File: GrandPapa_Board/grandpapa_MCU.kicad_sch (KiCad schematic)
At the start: 19 parts, among them J6 Conn_02x06, U10 MCP2515, U8 PIC18F26K83, Y1 12MHz

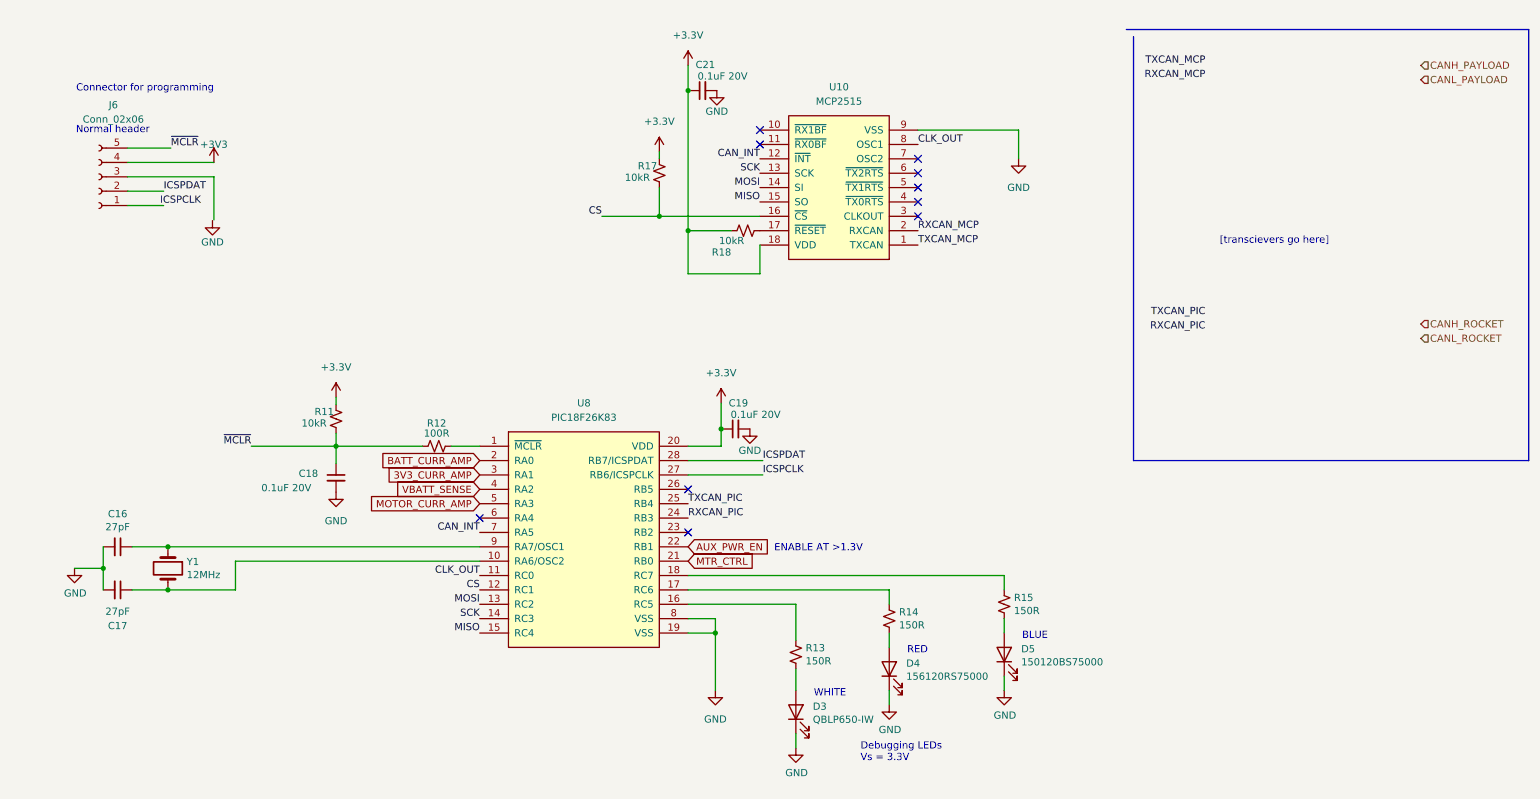
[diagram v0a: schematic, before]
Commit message: Remove 3.3V, placeholders for battery charge IC and 5V boost converter
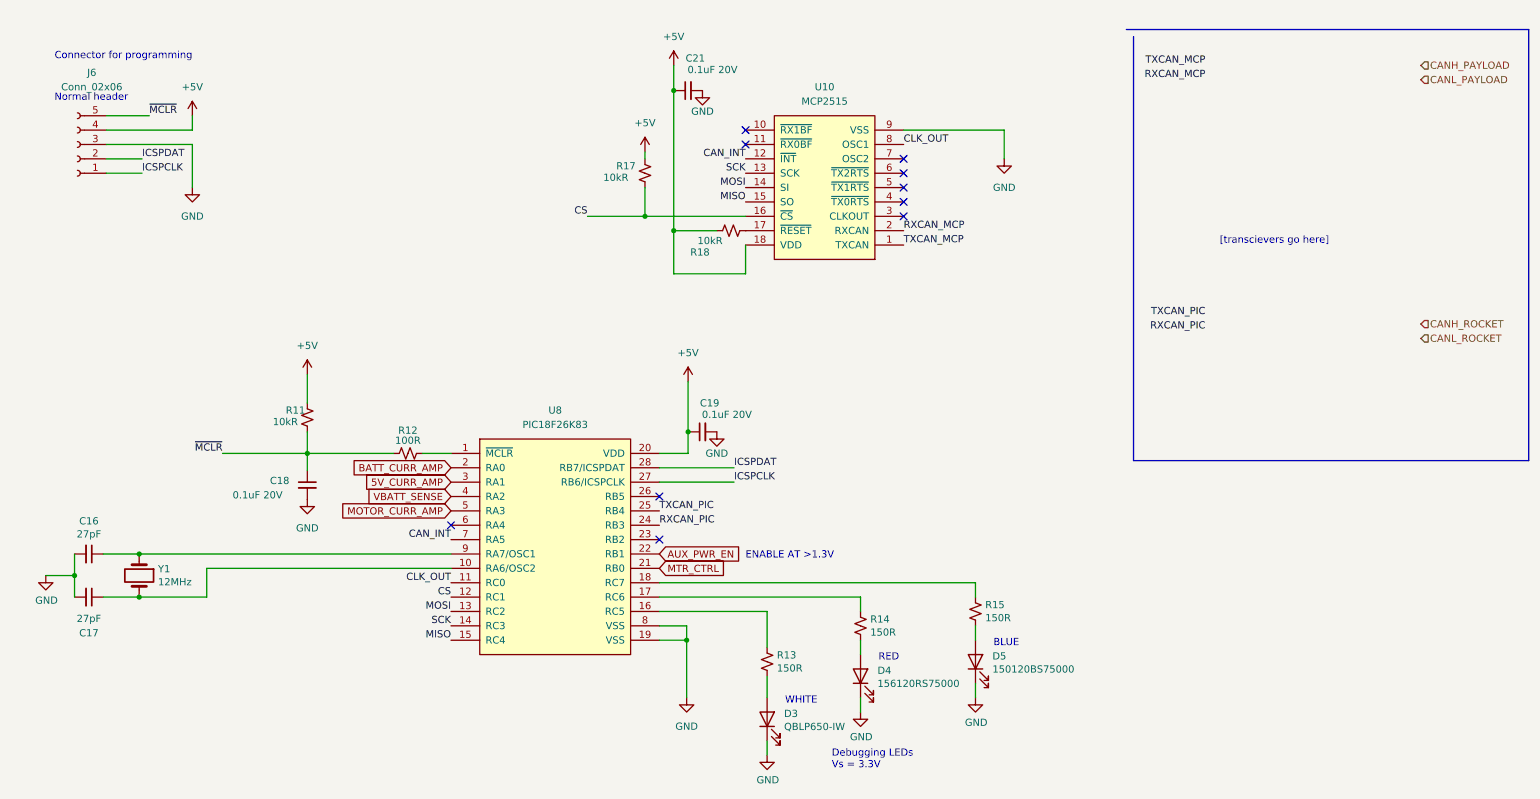
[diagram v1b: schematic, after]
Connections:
- net GND: now also J6.3 (Pin_3)
- net +3V3 renamed +5V
- net 3V3_CURR_AMP renamed 5V_CURR_AMP
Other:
- moved on the sheet: C16, C17, C18, C19, C21, D3, D4, D5, J6, R11, R12, R13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

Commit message: add 5V boost converter and 12V load switch, finish battery charge circuit
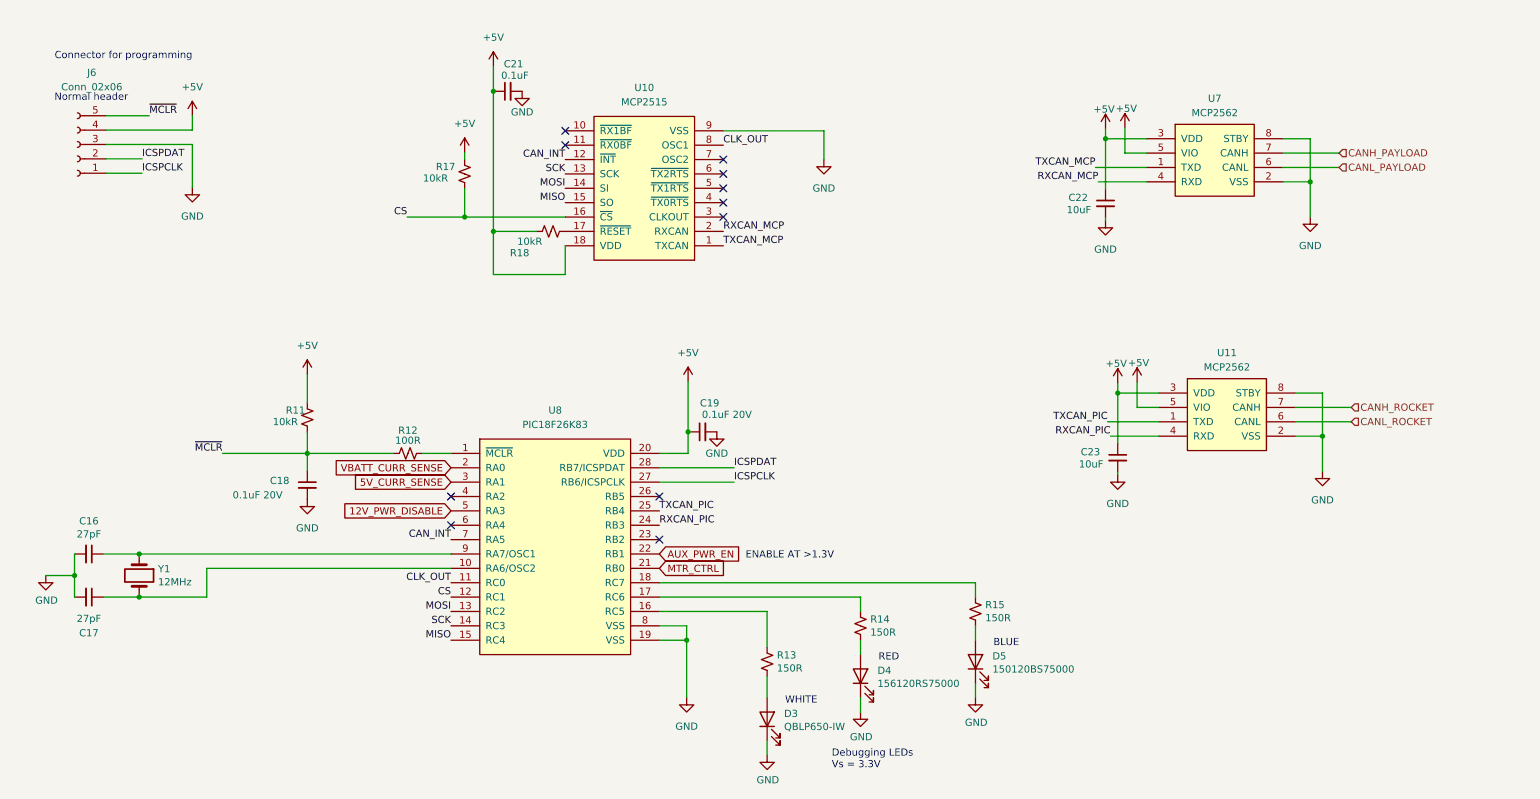
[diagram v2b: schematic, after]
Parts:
- added C22, C23: 10uF, symbol Device:C_Small
- added U11, U7: MCP2562, symbol CANHW:MCP2562
- C21: value 0.1uF 20V -> 0.1uF
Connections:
- net +5V: now also C22.1, C23.1, U11.3 (VDD), U11.5 (VIO), U7.3 (VDD), U7.5 (VIO)
- net CANH_PAYLOAD: now also U7.7 (CANH)
- net CANH_ROCKET: now also U11.7 (CANH)
- net CANL_PAYLOAD: now also U7.6 (CANL)
- net CANL_ROCKET: now also U11.6 (CANL)
- net GND: now also C22.2, C23.2, U11.2 (VSS), U11.8 (STBY), U7.2 (VSS), U7.8 (STBY)
- net RXCAN_MCP: now also U7.4 (RXD)
- net RXCAN_PIC: now also U11.4 (RXD)
- net TXCAN_MCP: now also U7.1 (TXD)
- net TXCAN_PIC: now also U11.1 (TXD)
- net 5V_CURR_AMP renamed 5V_CURR_SENSE
- net BATT_CURR_AMP renamed VBATT_CURR_SENSE
- net MOTOR_CURR_AMP renamed 12V_PWR_DISABLE
- net VBATT_SENSE: no longer names the net of U8.4 (RA2)
- no-connect marks 10 -> 11
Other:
- note removed: "[transcievers go here]"
- moved on the sheet: C21, R17, R18, U10

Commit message: clean up schematic, fix some ERC errors
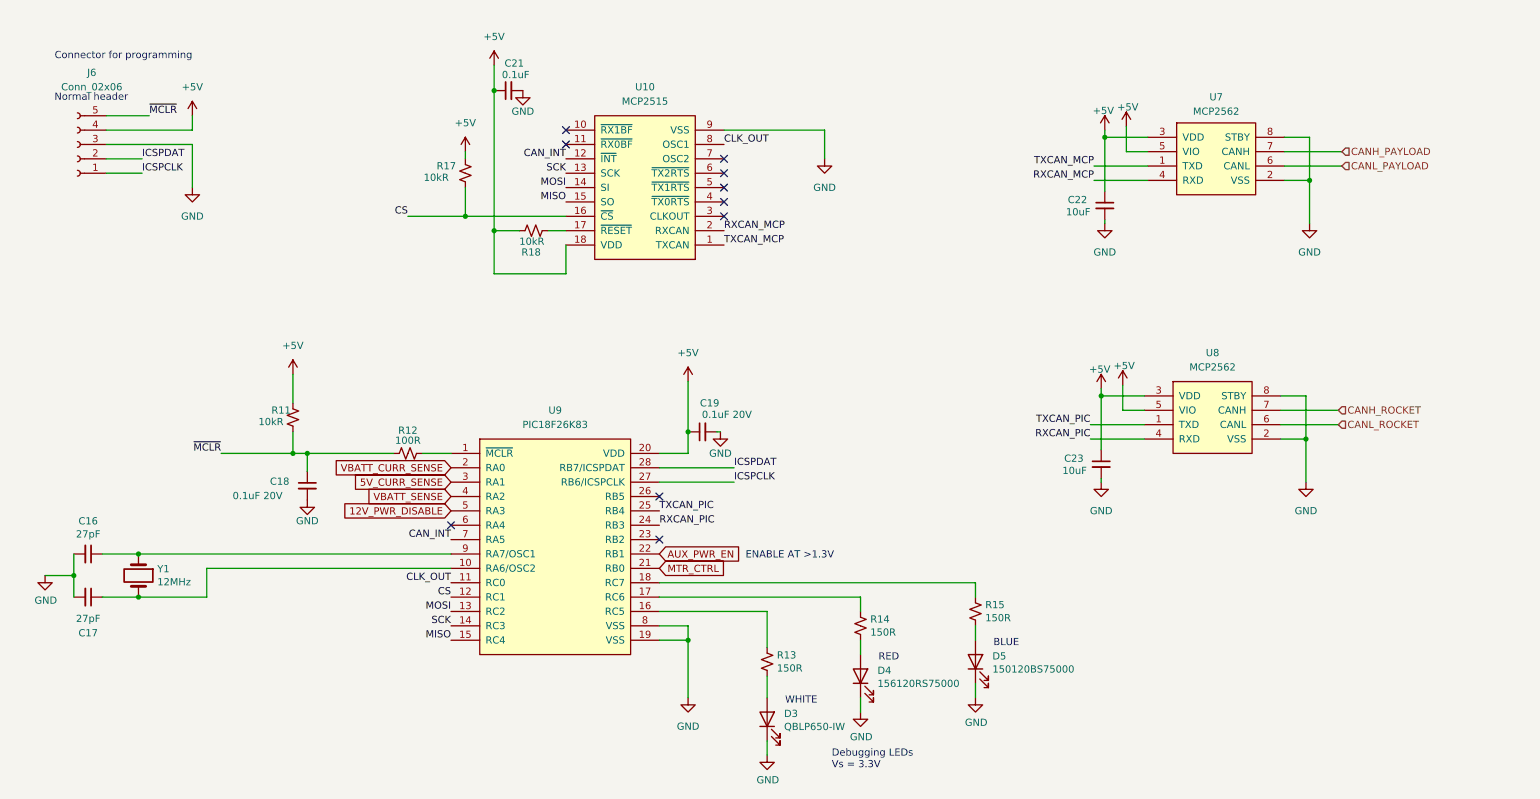
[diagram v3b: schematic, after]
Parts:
- removed U11: MCP2562, symbol CANHW:MCP2562
- added U8: MCP2562, symbol CANHW:MCP2562
- renumbered U8 to U9
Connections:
- net +5V: now also U8.3 (VDD), U8.5 (VIO)
- net CANH_ROCKET: now also U8.7 (CANH)
- net CANL_ROCKET: now also U8.6 (CANL)
- net GND: now also U8.2 (VSS), U8.8 (STBY)
- net RXCAN_PIC: now also U8.4 (RXD)
- net TXCAN_PIC: now also U8.1 (TXD)
- net VBATT_SENSE: now reaches U9.4 (RA2)
- no-connect marks 11 -> 10
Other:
- moved on the sheet: R11, R18

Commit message: move 12V shutoff to reg, rm motor stuff, subsheet/global pin redesign
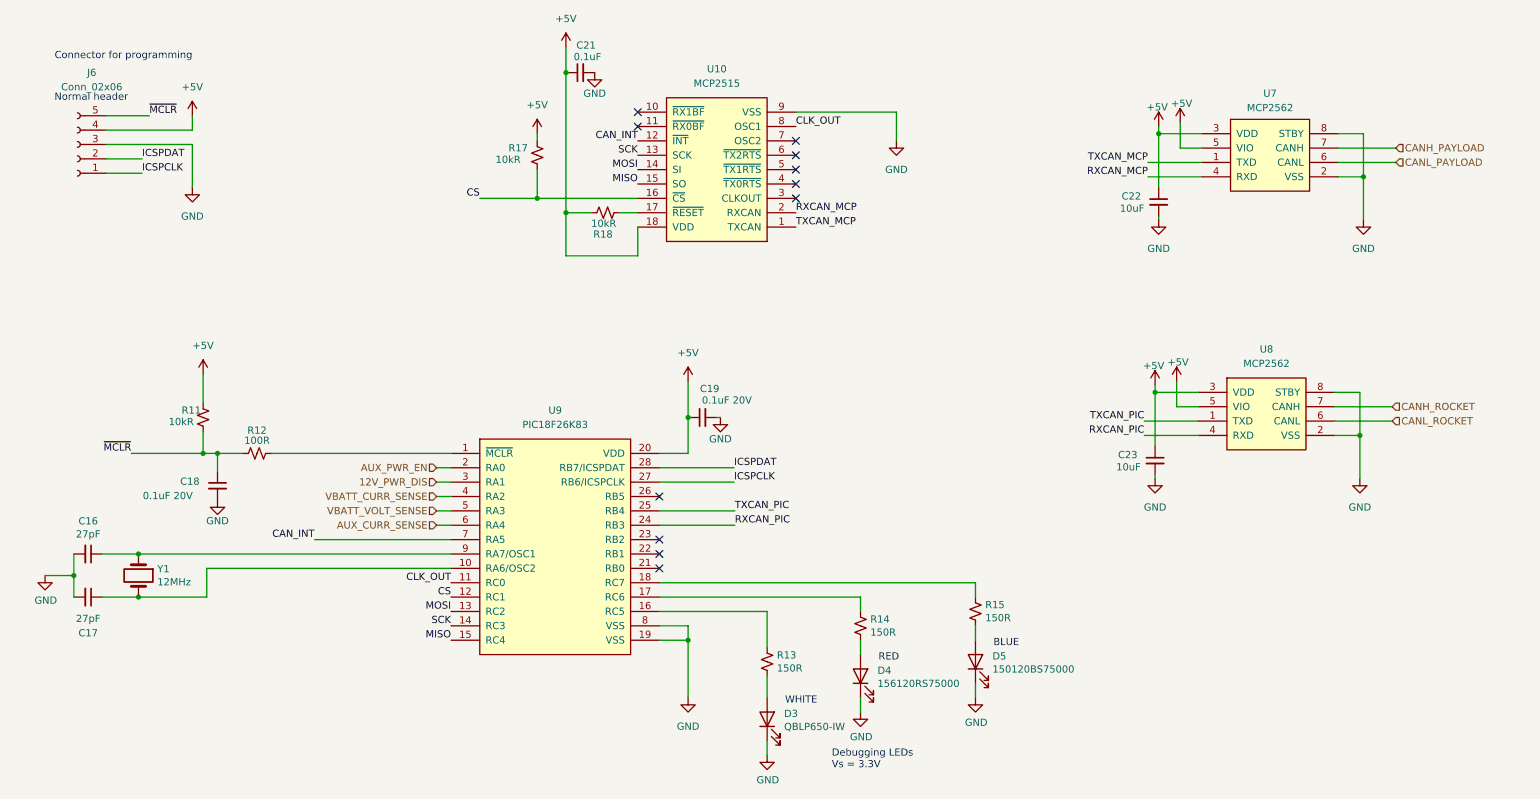
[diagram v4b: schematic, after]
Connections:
- net VBATT_SENSE is gone; now on net VBATT_CURR_SENSE: U9.4 (RA2)
- net AUX_PWR_EN: now also U9.2 (RA0); no longer U9.22 (RB1)
- net VBATT_CURR_SENSE: no longer U9.2 (RA0)
- net AUX_CURR_SENSE: now reaches U9.6 (RA4)
- net 12V_PWR_DISABLE renamed VBATT_VOLT_SENSE
- net 5V_CURR_SENSE renamed 12V_PWR_DIS
- net MTR_CTRL: no longer names the net of U9.21 (RB0)
- no-connect marks 10 -> 11
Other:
- note removed: "ENABLE AT >1.3V"
- moved on the sheet: C18, C19, C21, C22, C23, R11, R12, R17, R18, U10, U7, U8
